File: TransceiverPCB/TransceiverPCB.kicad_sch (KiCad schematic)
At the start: 0 parts

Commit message: Updated Readme, added parts
- 3d models were selected
- basic components dropped onto the schematic
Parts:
- added FL1, FL2: B39921B2672P810, B39921B2672P810, symbol LIB_IRISHSAT:B39921B2672P810
- added IC1: QPL6220QTR7, SON50P200X200X90-9N-D, symbol LIB_IRISHSAT:QPL6220QTR7
- added IC2: AD9218BSTZ-65, QFP50P900X900X160-48N, symbol LIB_IRISHSAT:AD9218BSTZ-65
- added IC3: AD9763ASTZ, QFP50P900X900X160-48N, symbol LIB_IRISHSAT:AD9763ASTZ
- added IC4: ADF4351BCPZ-RL7, QFN50P500X500X80-33N-D, symbol LIB_IRISHSAT:ADF4351BCPZ-RL7
- added U1: XC7A35T-1FTG256C, FT/FTG256ARTIX-7_AMD, symbol LIB_IRISHSAT:XC7A35T-1FTG256C
- added U2, U3: W25Q32JVSSIQ, SOIC-8_5P28X5P28_WIN, symbol LIB_IRISHSAT:W25Q32JVSSIQ
- added U4: DSC1001CI2-100.0000T, CDFN4_3P2X2P5_MCH, symbol LIB_IRISHSAT:DSC1001CI2-100.0000T
- added U5: ADL5380ACPZ-R7, CP_24_3_ADI, symbol LIB_IRISHSAT:ADL5380ACPZ-R7
- added U6: ADL5375-05ACPZ-R7, CP_24_7_ADI, symbol LIB_IRISHSAT:ADL5375-05ACPZ-R7
- added U7: ADA4940-2ACPZ-R7, CP_24_7_ADI, symbol LIB_IRISHSAT:ADA4940-2ACPZ-R7
- added U8: ADL5320ARKZ-R7, RK_3_ADI, symbol LIB_IRISHSAT:ADL5320ARKZ-R7
- added X1: ABM8-272-T3, ABM8-272-T3_ABR, symbol LIB_IRISHSAT:ABM8-272-T3
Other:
- note added: "ADC"
- note added: "ADC Driver"
- note added: "BPF"
- note added: "DAC"
- note added: "FDA"
- note added: "FPGA"
- note added: "FPGA Crystal Oscillator"
- note added: "FPGA Flash"
- note added: "IQ Demodulator"
- note added: "IQ Modulator"
- note added: "LNA"
- note added: "LO"
- note added: "PA"
- note added: "RP2040 Crystal Oscillator"
- note added: "RP2040 Flash"

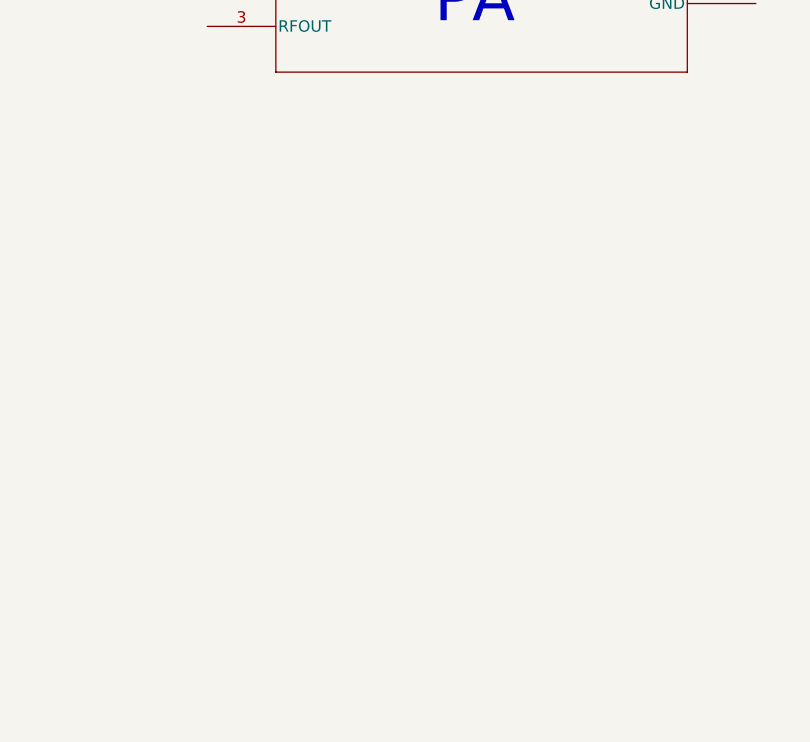
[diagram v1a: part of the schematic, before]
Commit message: Added USB-C
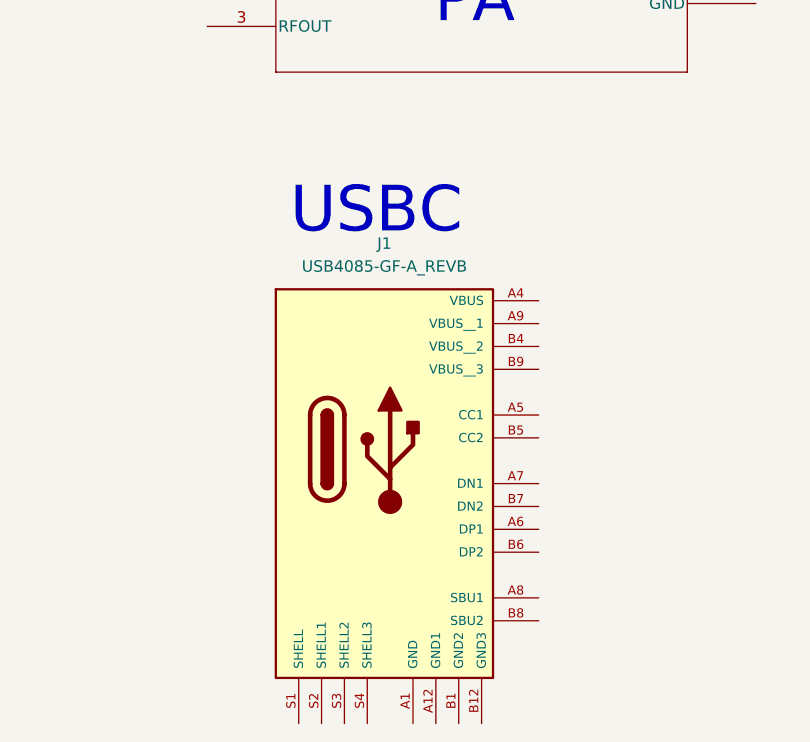
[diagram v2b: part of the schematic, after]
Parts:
- added J1: USB4085-GF-A_REVB, USB4085-GF-A_REVB:GCT_USB4085-GF-A_REVB, symbol LIB_IRISHSAT:USB4085-GF-A_REVB
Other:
- note added: "USBC"
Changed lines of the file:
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@@
+		)
+	)
+	(text "USBC"
+		(exclude_from_sim no)
+		(at 975.106 465.074 0)
+		(effects
+			(font
+				(size 5.08 5.08)
+			)
 		)
 	)
@@
 				)
 			)
+		)
+	)
+	(symbol
+		(lib_id "LIB_IRISHSAT:USB4085-GF-A_REVB")
+		(at 969.01 491.49 0)
+		(unit 1)
+		(exclude_from_sim no)
+		(in_bom yes)
+		(on_board yes)
+		(dnp no)
+		(fields_autoplaced yes)
+		(property "Reference" "J1"
+			(at 975.995 468.63 0)
+			(effects
+				(font
+					(size 1.27 1.27)
+				)
+			)
+		)
+		(property "Value" "USB4085-GF-A_REVB"
+			(at 975.995 471.17 0)
+			(effects
+				(font
+					(size 1.27 1.27)
+				)
+			)
+		)
+		(property "Footprint" "USB4085-GF-A_REVB:GCT_USB4085-GF-A_REVB"
+			(at 969.01 491.49 0)
+			(effects
+				(font
+					(size 1.27 1.27)
+				)
+				(justify bottom)
+				(hide yes)
+			)
+		)
+		(property "Datasheet" ""
+			(at 969.01 491.49 0)
+			(effects
+				(font
+					(size 1.27 1.27)
+				)
+				(hide yes)
+			)
+		)
+		(property "Description" ""
+			(at 969.01 491.49 0)
+			(effects
+				(font
+					(size 1.27 1.27)
+				)
+				(hide yes)
+			)
+		)
+		(property "PARTREV" "B"
+			(at 969.01 491.49 0)
+			(effects
+				(font
+					(size 1.27 1.27)
+				)
+				(justify bottom)
+				(hide yes)
+			)
+		)
+		(property "STANDARD" "Manufacturer Recommendations"
+			(at 969.01 491.49 0)
+			(effects
+				(font
+					(size 1.27 1.27)
+				)
+				(justify bottom)
+				(hide yes)
+			)
+		)
+		(property "SNAPEDA_PN" "USB4085-GF-A"
+			(at 969.01 491.49 0)
+			(effects
+				(font
+					(size 1.27 1.27)
+				)
+				(justify bottom)
+				(hide yes)
+			)
+		)
+		(property "MAXIMUM_PACKAGE_HEIGHT" "3.16mm"
+			(at 969.01 491.49 0)
+			(effects
+				(font
+					(size 1.27 1.27)
+				)
+				(justify bottom)
+				(hide yes)
+			)
+		)
+		(property "MANUFACTURER" "Global Connector Technology"
+			(at 969.01 491.49 0)
+			(effects
+				(font
+					(size 1.27 1.27)
+				)
+				(justify bottom)
+				(hide yes)
+			)
+		)
+		(pin "S1"
+		)
+		(pin "A1"
+		)
+		(pin "A4"
+		)
+		(pin "A9"
+		)
+		(pin "B4"
+		)
+		(pin "B9"
+		)
+		(pin "A5"
+		)
+		(pin "B5"
+		)
+		(pin "A7"
+		)
+		(pin "B7"
+		)
+		(pin "A6"
+		)
+		(pin "B6"
+		)
+		(pin "A8"
+		)
+		(pin "B8"
+		)
+		(pin "S2"
+		)
+		(pin "S3"
+		)
+		(pin "S4"
+		)
+		(pin "A12"
+		)
+		(pin "B1"
+		)
+		(pin "B12"
+		)
+		(instances
+			(project ""
+				(path "/c3b39813-b92f-4147-9d23-d3b5683e1da6"
+					(reference "J1")
+					(unit 1)
+				)
+			)

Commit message: Starting KiCAD
- Connected RP2040 to Flash
- Connected USB to RP2040
- Connected 12MHz crystal oscillator to RP2040
- Basic connections between many of the RF components
- Placed NC and GND
- Updated symbols to have some descriptions
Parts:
- added C1, C2, C3, C4, C5, C8: 100pF, symbol Device:C
- added C10, C11: 22pF, symbol Device:C
- added C6, C7: 0.1uF, symbol Device:C
- added C9: 100nF, symbol Device:C
- added FL3, FL4: B39921B2672P810, B39921B2672P810, symbol LIB_IRISHSAT:B39921B2672P810
- added J2, J3: RFPC-SMA27-F, RFPC-SMA27-F:GRADCONN_RFPC-SMA27-F, symbol LIB_IRISHSAT:RFPC-SMA27-F
- added R1: 1.5k, symbol Device:R_US
- added R2: DNF, symbol Device:R_US
- added R3, R5: 1k, symbol Device:R_US
- added R4: 10k, symbol Device:R_US
- added R6, R7: 5.1k, symbol Device:R_US
- added R8, R9: 27.4k, symbol Device:R_US
- added SW1, SW2: SW_Push, symbol Switch:SW_Push
- added U9: SC09147, QFN56_7X7_RPI, symbol LIB_IRISHSAT:SC09147
- U1: footprint FT/FTG256ARTIX-7_AMD -> LIB_IRISHSAT:FT&slash_FTG256ARTIX-7_AMD
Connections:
- net XIN_RP2040: now reaches X1.1 (IN)
- net XIN_RP2040: now also C11.1, U9.20 (XIN)
- net GND: now reaches X1.2 (GND)
- net GND: now also FL1.2 (GROUND_1), FL1.3 (GROUND_2), FL1.5 (GROUND_3), FL2.2 (GROUND_1), FL2.3 (GROUND_2), FL2.5 (GROUND_3), IC1.9 (GND), IC2.1 (GND_1), IC2.12 (GND_2), IC2.16 (GND_3), IC2.27 (GND_4), IC2.29 (GND_5), IC2.32 (GND_6), IC2.34 (GND_7), IC2.45 (GND_8), J1.A1 (GND), J1.A12 (GND1), J1.B1 (GND2), J1.B12 (GND3), J1.S1 (SHELL), J1.S2 (SHELL1), J1.S3 (SHELL2), J1.S4 (SHELL3), U3.4 (GND), U5.1 (GND3), U5.11 (GND4), U5.14 (GND2), U5.17 (GND2), U5.18 (GND3), U5.2 (GND1), U5.20 (GND3), U5.23 (GND3), U5.25 (EP), U5.5 (GND1), U5.7 (ENBL), U5.8 (GND4), U6.1 (DSOP), U6.11 (COMM), U6.12 (COMM), U6.13 (NC), U6.14 (COMM), U6.15 (NC), U6.17 (COMM), U6.19 (COMM), U6.2 (COMM), U6.20 (COMM), U6.23 (COMM), U6.25 (EP), U6.5 (COMM), U6.6 (NC), U6.7 (NC), U6.8 (COMM), U8.2 (GND), X1.4 (GND), C10.2, C11.2, C9.1, FL3.2 (GROUND_1), FL3.3 (GROUND_2), FL3.5 (GROUND_3), FL4.2 (GROUND_1), FL4.3 (GROUND_2), FL4.5 (GROUND_3), J2.G1, J2.G2, J2.G3, J2.G4, J3.G1, J3.G2, J3.G3, J3.G4, R6.2, R7.1, SW1.1, SW2.1, U9.19 (TESTEN), U9.57 (GND)
- net at X1.3 (OUT): now also C10.1, R3.1
- net LO_A_OUT+: now reaches IC4.12 (RFOUTA+)
- net LO_A_OUT+: now also C1.1
- net LO_A_OUT-: now reaches IC4.13 (RFOUTA-)
- net LO_A_OUT-: now also C2.1
- net LO_B_OUT+: now reaches IC4.14 (RFOUTB+)
- net LO_B_OUT+: now also C3.1
- net LO_B_OUT-: now reaches IC4.15 (RFOUTB-)
- net LO_B_OUT-: now also C4.1
- net at J1.A5 (CC1): now also R6.1
- net USB_D+: now reaches J1.A6 (DP1)
- net USB_D+: now also J1.B6 (DP2), R8.1
- net USB_D-: now reaches J1.A7 (DN1)
- net USB_D-: now also J1.B7 (DN2), R9.1
- net at J1.B5 (CC2): now also R7.2
- net at U5.10 (LOIN): now also C4.2
- net at U5.19 (ADJ): now also R1.2
- net at U5.9 (LOIP): now also C3.2
- net QSPI_SS_RP2040: now reaches U3.1 (/CS)
- net QSPI_SS_RP2040: now also R2.2, R5.1, U9.56 (SQPI_SS_N)
- net QSPI_SD1_RP2040: now reaches U3.2 (DO(IO1))
- net QSPI_SD1_RP2040: now also U9.55 (SQPI_SD1)
- net QSPI_SD2_RP2040: now reaches U3.3 (/WP(IO2))
- net QSPI_SD2_RP2040: now also U9.54 (SQPI_SD2)
- net QSPI_SD0_RP2040: now reaches U3.5 (DI(IO0))
- net QSPI_SD0_RP2040: now also U9.53 (SQPI_SD0)
- net QSPI_SCLK_RP2040: now reaches U3.6 (CLK)
- net QSPI_SCLK_RP2040: now also U9.52 (SQPI_SCLK)
- net QSPI_SD3_RP2040: now reaches U3.7 (/HOLD_OR_/RESET(IO3))
- net QSPI_SD3_RP2040: now also U9.51 (SQPI_SD3)
- net +3.3V: now reaches U3.8 (VCC)
- net +3.3V: now also C9.2, R2.1, R4.2
- net PA_IN: now reaches U8.1 (RFIN)
- net PA_IN: now also FL3.4 (OUTPUT)
- net PA_OUT: now reaches U8.3 (RFOUT)
- net PA_OUT: now also FL1.1 (INPUT)
- net LNA_IN: now reaches IC1.2 (RF_IN)
- net LNA_IN: now also FL4.4 (OUTPUT)
- net LNA_OUT: now reaches IC1.7 (RF_OUT)
- net LNA_OUT: now also FL2.1 (INPUT)
- net MOD_OUT: now reaches U6.16 (RFOUT)
- net MOD_OUT: now also FL3.1 (INPUT)
- net at U6.18 (VPS1): now also C5.2, C6.2
- net at U6.24 (VPS2): now also C7.1, C8.1
- net at U6.3 (LOIP): now also C1.2
- net at U6.4 (LOIN): now also C2.2
- net SMA_TX_IN: now reaches FL1.4 (OUTPUT)
- net SMA_TX_IN: now also J2.1
- net DEMOD_RF_IN: now reaches FL2.4 (OUTPUT)
- new net: R8.2, U9.47 (USB_DP)
- new net: R9.2, U9.46 (USB_DM)
- new net RUN: R4.1, SW1.2, U9.26 (RUN)
- new net SMA_RX_OUT: FL4.1 (INPUT), J3.1
- new net USB_BOOT: R5.2, SW2.2
- new net XOUT_RP2040: R3.2, U9.21 (XOUT)
- no-connect marks 0 -> 15
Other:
- note added: "Ctrl logic?"
- note added: "LPF"
- note added: "Needs a balun"
- note removed: "ADC"
- note removed: "ADC Driver"
- note removed: "BPF"
- note removed: "DAC"
- note removed: "FDA"
- note removed: "FPGA"
- note removed: "FPGA Crystal Oscillator"
- note removed: "FPGA Flash"
- note removed: "IQ Demodulator"
- note removed: "IQ Modulator"
- note removed: "LNA"
- note removed: "LO"
- note removed: "PA"
- note removed: "RP2040 Crystal Oscillator"
- note removed: "RP2040 Flash"
- note removed: "USBC"

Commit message: Finished RP2040 power supply
- power of RP2040
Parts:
- added C12, C26, C29: 10uF, symbol Device:C
- added C13, C21, C24, C25: 1uF, symbol Device:C
- added C14, C15, C16, C17, C18, C19, C20, C22, C23: 100nF, symbol Device:C
- added C27, C28: 0.1uF, symbol Device:C
- added D1: ESD5Z5V0, LIB_IRISHSAT:P38_SOD-523, symbol LIB_IRISHSAT:ESD5Z5V0
- added L1: BLM21PG600SN1D, LIB_IRISHSAT:IND_BLM21_MUR, symbol LIB_IRISHSAT:BLM21PG600SN1D
- added R10: 10k, symbol Device:R_US
- added U10: AP2112K-3.3TRG1, SOT_RG1_DIO, symbol LIB_IRISHSAT:AP2112K-3.3TRG1
- added U11: LM66100DCKR, DCK6_TEX, symbol LIB_IRISHSAT:LM66100DCKR
- J2, J3: footprint RFPC-SMA27-F:GRADCONN_RFPC-SMA27-F -> LIB_IRISHSAT:GRADCONN_RFPC-SMA27-F
- U1: footprint LIB_IRISHSAT:FT&slash_FTG256ARTIX-7_AMD -> FT/FTG256ARTIX-7_AMD
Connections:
- net +3.3V is gone; now on net +3V3: C9.2, R2.1, R4.2, U3.8 (VCC)
- net GND: now also C12.1, C13.2, C14.2, C15.2, C16.2, C17.2, C18.2, C19.2, C20.2, C21.1, C22.1, C23.1, C24.1, C25.1, C26.1, C27.1, C28.1, C29.1, D1.2 (C), U10.2 (GND), U11.2 (GND), U11.3 (*CE), U11.5 (ST)
- net +5V: now reaches J1.A4 (VBUS)
- net +5V: now also J1.A9 (VBUS__1), J1.B4 (VBUS__2), J1.B9 (VBUS__3), C12.2, D1.1 (A), L1.2
- net +3V3: now reaches U9.1 (IOVDD)
- net +3V3: now also U9.10 (IOVDD), U9.22 (IOVDD), U9.33 (IOVDD), U9.42 (IOVDD), U9.43 (ADC_AVDD), U9.44 (VREG_VIN), U9.48 (USB_VDD), U9.49 (IOVDD), C13.1, C14.1, C15.1, C16.1, C17.1, C18.1, C19.1, C20.1, C24.2, C28.2, C29.2, U10.5 (VOUT)
- net +1V1: now reaches U9.23 (DVDD)
- net +1V1: now also U9.45 (VREG_VOUT), U9.50 (DVDD), C21.2, C22.2, C23.2
- new net: C25.2, C26.2, C27.2, R10.1, U10.1 (VIN), U11.6 (VOUT)
- new net: L1.1, U11.1 (VIN)
- new net: R10.2, U10.3 (EN)
- no-connect marks 15 -> 48
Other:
- note added: "USB to 3.3V with Filters and Protection"
- moved on the sheet: C10, C11, C9, J1, R2, R3, R4, R5, R6, R7, R8, R9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

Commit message: Diode Fix
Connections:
- net +5V: now also D1.2 (C); no longer D1.1 (A)
- net GND: now also D1.1 (A); no longer D1.2 (C)
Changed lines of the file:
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@@
 	)
 	(junction
-		(at 33.02 561.34)
-		(diameter 0)
-		(color 0 0 0 0)
-	)
-	(junction
 		(at 27.94 514.35)
 		(diameter 0)
@@
 		(color 0 0 0 0)
 	)
+	(junction
+		(at 33.02 561.34)
+		(diameter 0)
+		(color 0 0 0 0)
+	)
 	(no_connect
 		(at 171.45 563.88)
@@
 	(wire
 		(pts
-			(xy 33.02 561.34) (xy 39.37 561.34)
-		)
-		(stroke
-			(width 0)
-			(type default)
-		)
-	)
-	(wire
-		(pts
 			(xy 506.73 137.16) (xy 506.73 147.32)
 		)
@@
 	(wire
 		(pts
+			(xy 33.02 561.34) (xy 39.37 561.34)
+		)
+		(stroke
+			(width 0)
+			(type default)
+		)
+	)
+	(wire
+		(pts
 			(xy 54.61 467.36) (xy 54.61 469.9)
 		)
@@
 		(lib_id "LIB_IRISHSAT:ESD5Z5V0")
 		(at 33.02 557.53 270)
-		(mirror x)
 		(unit 1)
 		(exclude_from_sim no)
@@
 		(dnp no)
 		(property "Reference" "D1"
-			(at 30.48 556.2599 90)
+			(at 30.48 558.8001 90)
 			(effects
 				(font
@@
 		)
 		(property "Value" "ESD5Z5V0"
-			(at 30.48 558.7999 90)
+			(at 30.48 556.2601 90)
 			(effects
 				(font

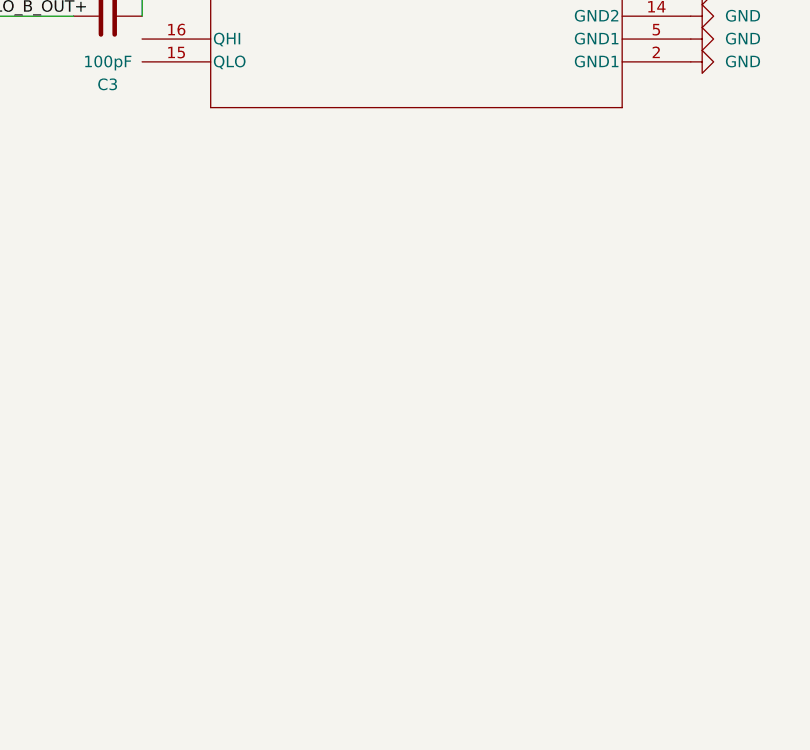
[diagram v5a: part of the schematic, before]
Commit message: Added the AD__87 Demod
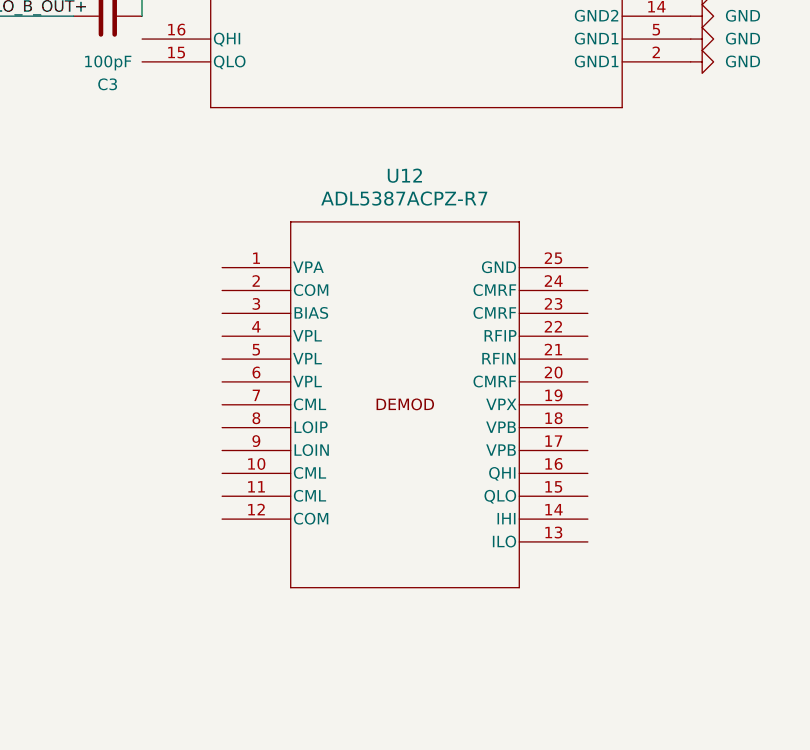
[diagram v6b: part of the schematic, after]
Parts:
- added U12: ADL5387ACPZ-R7, CP-24-14_ADI, symbol LIB_IRISHSAT:ADL5387ACPZ-R7
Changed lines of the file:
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@@
+	)
+	(symbol
+		(lib_id "LIB_IRISHSAT:ADL5387ACPZ-R7")
+		(at 469.9 350.52 0)
+		(unit 1)
+		(exclude_from_sim no)
+		(in_bom yes)
+		(on_board yes)
+		(dnp no)
+		(fields_autoplaced yes)
+		(property "Reference" "U12"
+			(at 490.22 340.36 0)
+			(effects
+				(font
+					(size 1.524 1.524)
+				)
+			)
+		)
+		(property "Value" "ADL5387ACPZ-R7"
+			(at 490.22 342.9 0)
+			(effects
+				(font
+					(size 1.524 1.524)
+				)
+			)
+		)
+		(property "Footprint" "CP-24-14_ADI"
+			(at 469.9 350.52 0)
+			(effects
+				(font
+					(size 1.27 1.27)
+					(italic yes)
+				)
+				(hide yes)
+			)
+		)
+		(property "Datasheet" "https://www.analog.com/media/en/technical-documentation/data-sheets/ADL5387.pdf"
+			(at 469.9 350.52 0)
+			(effects
+				(font
+					(size 1.27 1.27)
+					(italic yes)
+				)
+				(hide yes)
+			)
+		)
+		(property "Description" ""
+			(at 469.9 350.52 0)
+			(effects
+				(font
+					(size 1.27 1.27)
+				)
+				(hide yes)
+			)
+		)
+		(pin "24"
+		)
+		(pin "23"
+		)
+		(pin "22"
+		)
+		(pin "21"
+		)
+		(pin "20"
+		)
+		(pin "19"
+		)
+		(pin "18"
+		)
+		(pin "17"
+		)
+		(pin "16"
+		)
+		(pin "15"
+		)
+		(pin "14"
+		)
+		(pin "13"
+		)
+		(pin "25"
+		)
+		(pin "2"
+		)
+		(pin "3"
+		)
+		(pin "4"
+		)
+		(pin "5"
+		)
+		(pin "6"
+		)
+		(pin "7"
+		)
+		(pin "8"
+		)
+		(pin "9"
+		)
+		(pin "10"
+		)
+		(pin "11"
+		)
+		(pin "12"
+		)
+		(pin "1"
+		)
+		(instances
+			(project ""
+				(path "/c3b39813-b92f-4147-9d23-d3b5683e1da6"
+					(reference "U12")
+					(unit 1)
+				)
+			)
+		)
 	)
 	(symbol
